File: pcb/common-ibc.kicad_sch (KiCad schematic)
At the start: 96 parts, among them J1 XILINX_JTAG, J10 U.FL, J11 MOLEX_0039291087, J2 MOLEX_0039291067, J3 GROUND, J4 GROUND, J5 MOLEX_0532610571, J6 U.FL, J7 U.FL, J8 U.FL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

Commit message: Initial I2C server class implementation
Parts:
- added C27: DNP, symbol device:CP1
- added R27: DNP, symbol device:R
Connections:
- net 48V0: now also R27.2; no longer R1.2 (Vo)
- net GND: now also C27.2
- new net 48V0_SHOUT: C27.1, R1.2 (Vo), R27.1
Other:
- note added: "TODO: TPS16630 from 48V0_SHOUT to 48V0"
- moved on the sheet: C6, C7
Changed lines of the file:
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@@
 	)
 	(junction
+		(at 208.28 27.94)
+		(diameter 0)
+		(color 0 0 0 0)
+	)
+	(junction
 		(at 224.79 358.14)
 		(diameter 0)
@@
 	)
 	(junction
-		(at 167.64 27.94)
-		(diameter 0)
-		(color 0 0 0 0)
-	)
-	(junction
 		(at 224.79 177.8)
 		(diameter 0)
@@
 	)
 	(junction
+		(at 168.91 27.94)
+		(diameter 0)
+		(color 0 0 0 0)
+	)
+	(junction
 		(at 201.93 167.64)
 		(diameter 0)
@@
 	(wire
 		(pts
-			(xy 167.64 35.56) (xy 191.77 35.56)
+			(xy 208.28 35.56) (xy 232.41 35.56)
 		)
 		(stroke
@@
 	(wire
 		(pts
-			(xy 151.13 27.94) (xy 167.64 27.94)
-		)
-		(stroke
-			(width 0)
-			(type default)
-		)
-	)
-	(wire
-		(pts
 			(xy 262.89 257.81) (xy 250.19 257.81)
 		)
@@
 	(wire
 		(pts
+			(xy 168.91 27.94) (xy 184.15 27.94)
+		)
+		(stroke
+			(width 0)
+			(type default)
+		)
+	)
+	(wire
+		(pts
 			(xy 165.1 369.57) (xy 165.1 372.11)
 		)
@@
 	(wire
 		(pts
+			(xy 191.77 27.94) (xy 208.28 27.94)
+		)
+		(stroke
+			(width 0)
+			(type default)
+		)
+	)
+	(wire
+		(pts
 			(xy 224.79 355.6) (xy 224.79 358.14)
 		)
@@
 	(wire
 		(pts
+			(xy 151.13 27.94) (xy 168.91 27.94)
+		)
+		(stroke
+			(width 0)
+			(type default)
+		)
+	)
+	(wire
+		(pts
 			(xy 406.4 128.27) (xy 427.99 128.27)
 		)
@@
 	(wire
 		(pts
-			(xy 167.64 27.94) (xy 191.77 27.94)
+			(xy 208.28 27.94) (xy 232.41 27.94)
 		)
 		(stroke
@@
 		)
 	)
+	(text "TODO: TPS16630 from 48V0_SHOUT to 48V0"
+		(exclude_from_sim no)
+		(at 188.468 53.594 0)
+		(effects
+			(font
+				(size 1.27 1.27)
+			)
+		)
+	)
 	(text "5V standby regulator\nThermally limited to 142 mA"
 		(exclude_from_sim no)
@@
 	)
 	(label "GND"
-		(at 191.77 35.56 0)
+		(at 232.41 35.56 0)
 		(fields_autoplaced yes)
 		(effects
@@
 		)
 	)
+	(label "GND"
+		(at 168.91 35.56 180)
+		(fields_autoplaced yes)
+		(effects
+			(font
+				(size 1.27 1.27)
+			)
+			(justify right bottom)
+		)
+	)
 	(label "3V3_SB"
 		(at 383.54 110.49 180)
@@
 		)
 	)
+	(label "48V0_SHOUT"
+		(at 152.4 27.94 0)
+		(fields_autoplaced yes)
+		(effects
+			(font
+				(size 1.27 1.27)
+			)
+			(justify left bottom)
+		)
+	)
 	(label "GND"
 		(at 101.6 132.08 180)
@@
 	)
 	(label "48V0"
-		(at 158.75 27.94 0)
+		(at 208.28 27.94 180)
 		(fields_autoplaced yes)
 		(effects
@@
 				(size 1.27 1.27)
 			)
-			(justify left bottom)
+			(justify right bottom)
 		)
 	)
@@
 	)
 	(symbol
+		(lib_id "device:R")
+		(at 187.96 27.94 90)
+		(unit 1)
+		(exclude_from_sim no)
+		(in_bom yes)
+		(on_board yes)
+		(dnp no)
+		(fields_autoplaced yes)
+		(property "Reference" "R27"
+			(at 187.96 22.7795 90)
+			(effects
+				(font
+					(size 1.27 1.27)
+				)
+			)
+		)
+		(property "Value" "DNP"
+			(at 187.96 25.2038 90)
+			(effects
+				(font
+					(size 1.27 1.27)
+				)
+			)
+		)
+		(property "Footprint" ""
+			(at 187.96 29.718 90)
+			(effects
+				(font
+					(size 1.27 1.27)
+				)
+				(hide yes)
+			)
+		)
+		(property "Datasheet" ""
+			(at 187.96 27.94 0)
+			(effects
+				(font
+					(size 1.27 1.27)
+				)
+				(hide yes)
+			)
+		)
+		(property "Description" "Resistor"
+			(at 187.96 27.94 0)
+			(effects
+				(font
+					(size 1.27 1.27)
+				)
+				(hide yes)
+			)
+		)
+		(pin "1"
+		)
+		(pin "2"
+		)
+		(instances
+			(project "common-ibc"
+				(path "/20bfa5a1-b612-414f-859c-0b0904e97a2e"
+					(reference "R27")
+					(unit 1)
+				)
+			)
+		)
+	)
+	(symbol
 		(lib_id "device:C")
 		(at 68.58 294.64 90)
@@
 	(symbol
 		(lib_id "device:CP1")
-		(at 191.77 31.75 0)
+		(at 232.41 31.75 0)
 		(unit 1)
 		(exclude_from_sim no)
@@
 		(fields_autoplaced yes)
 		(property "Reference" "C7"
-			(at 194.691 29.9028 0)
+			(at 235.331 29.9028 0)
 			(effects
 				(font
@@
 		)
 		(property "Value" "EEH-ZU1J101V"
-			(at 194.691 32.3271 0)
+			(at 235.331 32.3271 0)
 			(effects
 				(font
@@
 		)
 		(property "Footprint" "azonenberg_pcb:CAP_AL_10MM_SMT"
-			(at 191.77 31.75 0)
+			(at 232.41 31.75 0)
 			(effects
 				(font
@@
 		)
 		(property "Datasheet" ""
-			(at 191.77 31.75 0)
+			(at 232.41 31.75 0)
 			(effects
 				(font
@@
 		)
 		(property "Description" ""
-			(at 191.77 31.75 0)
+			(at 232.41 31.75 0)
 			(effects
 				(font
@@
 	(symbol
 		(lib_id "device:CP1")
-		(at 167.64 31.75 0)
+		(at 208.28 31.75 0)
 		(unit 1)
 		(exclude_from_sim no)
@@
 		(dnp no)
 		(property "Reference" "C6"
-			(at 171.45 30.4831 0)
+			(at 212.09 30.4831 0)
 			(effects
 				(font
@@
 		)
 		(property "Value" "EEH-ZU1J101V"
-			(at 171.45 33.02 0)
+			(at 212.09 33.02 0)
 			(effects
 				(font
@@
 		)
 		(property "Footprint" "azonenberg_pcb:CAP_AL_10MM_SMT"
-			(at 167.64 31.75 0)
+			(at 208.28 31.75 0)
 			(effects
 				(font
@@
 		)
 		(property "Datasheet" ""
-			(at 167.64 31.75 0)
+			(at 208.28 31.75 0)
 			(effects
 				(font
@@
 		)
 		(property "Description" ""
-			(at 167.64 31.75 0)
+			(at 208.28 31.75 0)
 			(effects
 				(font
@@
 					(unit 1)
 				)
+			)
+		)
+	)
+	(symbol
+		(lib_id "device:CP1")
+		(at 168.91 31.75 0)
+		(unit 1)
+		(exclude_from_sim no)
+		(in_bom yes)
+		(on_board yes)
+		(dnp no)
+		(fields_autoplaced yes)
+		(property "Reference" "C27"
+			(at 171.831 29.9028 0)
+			(effects
+				(font
+					(size 1.27 1.27)
+				)
+				(justify left)
+			)
+		)
+		(property "Value" "DNP"
+			(at 171.831 32.3271 0)
+			(effects
+				(font
+					(size 1.27 1.27)
+				)
+				(justify left)
+			)
+		)
+		(property "Footprint" ""
+			(at 168.91 31.75 0)
+			(effects
+				(font
+					(size 1.27 1.27)
+				)
+				(hide yes)
+			)
+		)
+		(property "Datasheet" ""
+			(at 168.91 31.75 0)
+			(effects
+				(font
+					(size 1.27 1.27)
+				)
+				(hide yes)
+			)
+		)
+		(property "Description" "Polarised capacitor"
+			(at 168.91 31.75 0)
+			(effects
+				(font
+					(size 1.27 1.27)
+				)
+				(hide yes)
+			)
+		)
+		(pin "1"
+		)
+		(pin "2"
+		)
+		(instances
+			(project "common-ibc"
+				(path "/20bfa5a1-b612-414f-859c-0b0904e97a2e"
+					(reference "C27")
+					(unit 1)
+				)

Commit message: Hopefully-mostly-done v0.5 layout
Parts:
- added C28: 10 nF, azonenberg_pcb:EIA_0402_CAP_NOSILK, symbol device:C
- added R28: 806K, azonenberg_pcb:EIA_0603_RES_NOSILK, symbol device:R
- added R29: 620, azonenberg_pcb:EIA_0402_RES_NOSILK, symbol device:R
- added R30: 6.49K, azonenberg_pcb:EIA_0402_RES_NOSILK, symbol device:R
- added R33: 9.09K, azonenberg_pcb:EIA_0402_RES_NOSILK, symbol device:R
- added R34: 20K, azonenberg_pcb:EIA_0402_RES_NOSILK, symbol device:R
- added R35, R37: DNP, azonenberg_pcb:EIA_0402_RES_NOSILK, symbol device:R
- added R36: DNP, azonenberg_pcb:EIA_0603_RES_NOSILK, symbol device:R
- added R38: 17.8K, azonenberg_pcb:EIA_0402_RES_NOSILK, symbol device:R
- added TP2, TP3: TESTPOINT, azonenberg_pcb:TESTPOINT_SMT_0.5MM, symbol conn:CONN_01X01
- added U1: TPS16630, azonenberg_pcb:QFN_24_0.5MM_4x4MM, symbol power-azonenberg:TPS16630
- C24: footprint (none) -> azonenberg_pcb:EIA_1812_CAP_NOSILK
- C27: value DNP -> 875105945001; footprint (none) -> azonenberg_pcb:CAP_AL_6.3MM_SMT
- D6: footprint (none) -> azonenberg_pcb:SOD128
- D7: footprint (none) -> azonenberg_pcb:SMA
- R27: footprint (none) -> azonenberg_pcb:EIA_0805_CAP_NOSILK
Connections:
- net GND_RAW is gone; now on net GND: C24.2, D6.2 (A), D7.2 (A), J2.4 (GND), J2.5 (GND), J2.6 (GND)
- net 3V3_SB: now also U9.18 (PB0)
- net 48V0: now also U1.17 (OUT), U1.18 (OUT)
- net 48V0_SHOUT: now also R28.1, R36.2, U1.1 (IN), U1.2 (IN), U1.5 (P_IN)
- net GND: now also C28.2, R33.2, R34.2, R35.2, R37.2, R38.2, U1.8 (GND), U1.PAD (GND)
- net 48V0_IMON: now reaches U9.15 (PA5)
- net 48V0_IMON: now also R34.1, U1.13 (IMON)
- new net: R29.1, R30.2
- new net 48V0_FLT: TP3.1 (P1), U1.14 (~{FLT})
- new net 48V0_GOOD: TP2.1 (P1), U1.16 (PGOOD)
- new net C_SOFTSTART: C28.1, U1.9 (dVdT)
- new net ILIM: R33.1, U1.10 (ILIM)
- new net TPS_MODE: R35.1, U1.11 (MODE)
- new net TPS_SHDN: R36.1, R37.1, U1.12 (~{SHDN})
- new net VOVP: R29.2, R38.1, U1.7 (OVP)
- new net VUVLO: R28.2, R30.1, U1.6 (UVLO)
- no-connect marks 16 -> 14
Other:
- note added: "1.2V rising threshold (nominal) at each comaprator Total string resistance = 830.91K VOVP = 17.8K / 830.91K = 1/46.68 VUVLO = (17.8K + 620 + 6.49K) / 830.91K = 24.91K / 830.91K = 1/33.35 So VOVP = 56.0V +/- 1% VUVLO = 40.0V +/- 1%"
- note added: "48V0_IMON is new input from TPS present in rev 0.5 PCB only PB0 floating = rev 0.4 PB0 high = rev 0.5"
- note added: "If using current monitor feature of U1 instead of input high side shunt: * Replace R1 with 0R jumper * DNP U4, C11, L1, C13"
- note added: "Iinrush = 200 uF * 48V / tdVdT if we target 10 ms, that's 960 mA inrush. tdVdT = 20.8 * 1e3 * Vin * CdVdT"
- note added: "Max power is 72W = 1.5A Current limit to 2A 2A = 18K / Rilim Rilim = 9K"
- note added: "Populate R35 with 0R to enable auto retry on overload With R35 DNP, overcurrent results in output latching off"
- note added: "Populate either U1 (and support passives) or R27 with 0R, not both"
- note added: "R36/37 DNP assuming input is pulled high internally to 2.7V If insufficiently robust can add pullup/down network Must be >2.0V and <5.0V"
- note added: "Vimon = 27.9 uA/A * Iout * Rimon Across 20K ohms this is 558 mV/A"
- note removed: "TODO: TPS16630 from 48V0_SHOUT to 48V0"
- moved on the sheet: C6, C7

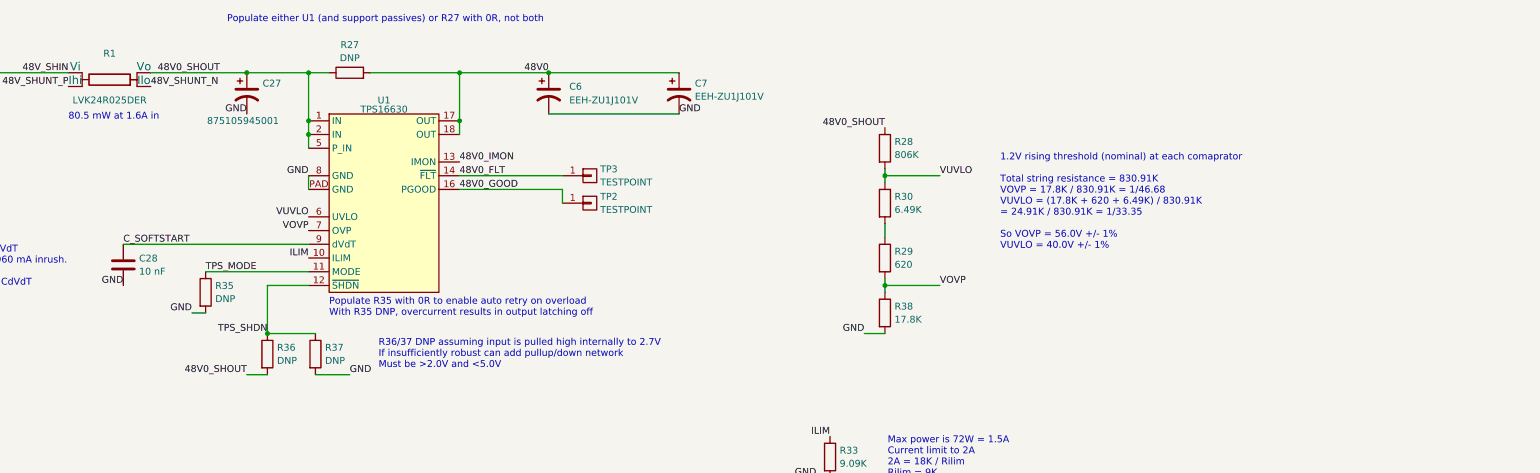
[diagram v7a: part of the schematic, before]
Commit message: Final v0.5 IBC design going to fab for quotes
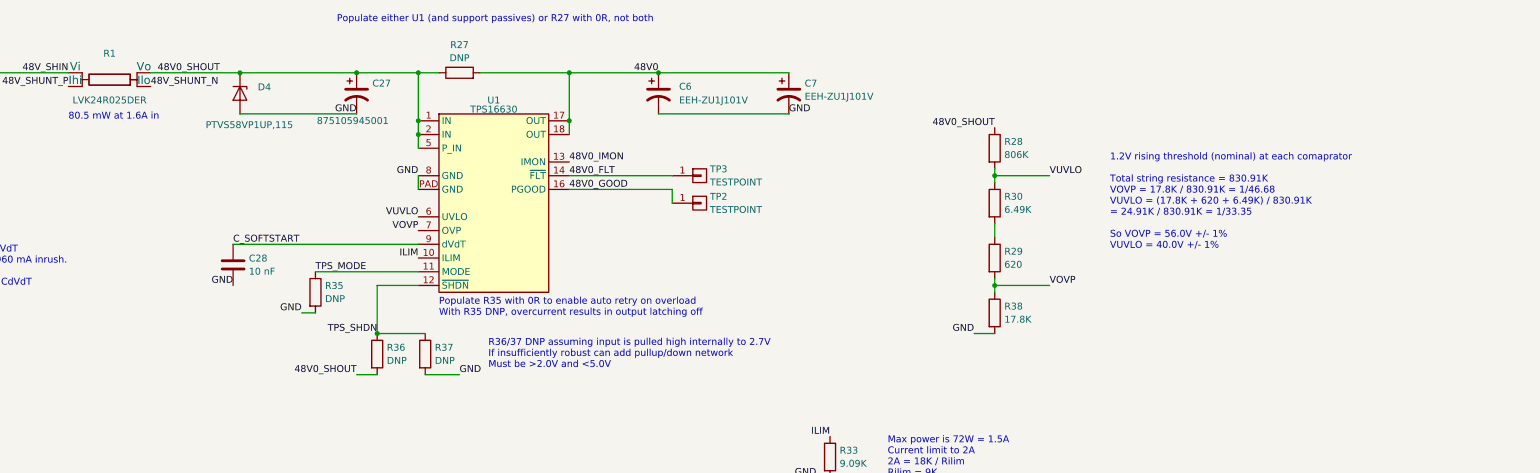
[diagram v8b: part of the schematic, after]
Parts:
- added D4: PTVS58VP1UP,115, azonenberg_pcb:SOD128, symbol device:D_Zener
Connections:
- net 48V0_SHOUT: now also D4.1 (K)
- net GND: now also D4.2 (A)
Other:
- moved on the sheet: C27, C28, C6, C7, R27, R28, R29, R30, R35, R36, R37, R38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
